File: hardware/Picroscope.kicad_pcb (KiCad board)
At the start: 4 copper layers, 38 x 63.5 mm, 75 parts, among them J1 USB_C_Receptacle_USB2.0_16P, J2 Conn_01x03_Pin, J3 HDMI_A, J4 Conn_02x09_Odd_Even, SW1 SMD_Pushbutton, SW2 SMD_Pushbutton, U1 RP2350B-QFN80, U2 W25Q32JVSS, U3 AMS1117-3.3, Y1 ABM8-272-T3

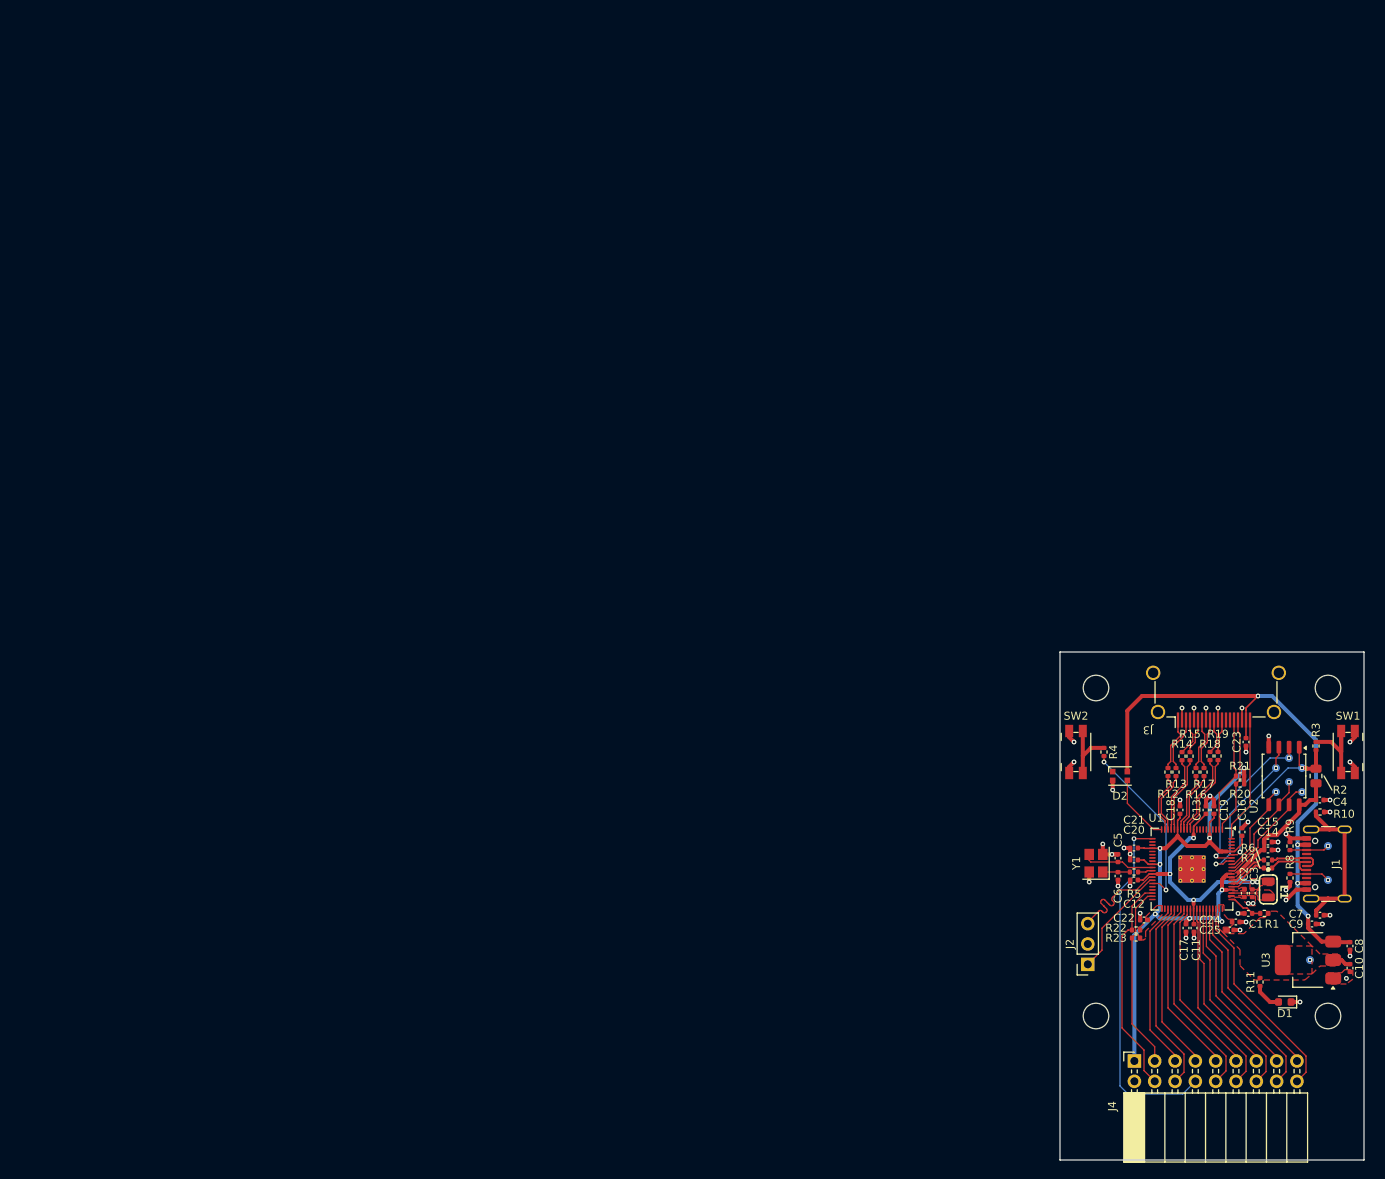
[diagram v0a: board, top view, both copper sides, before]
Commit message: added length tuning to 'crucial' traces except qspi
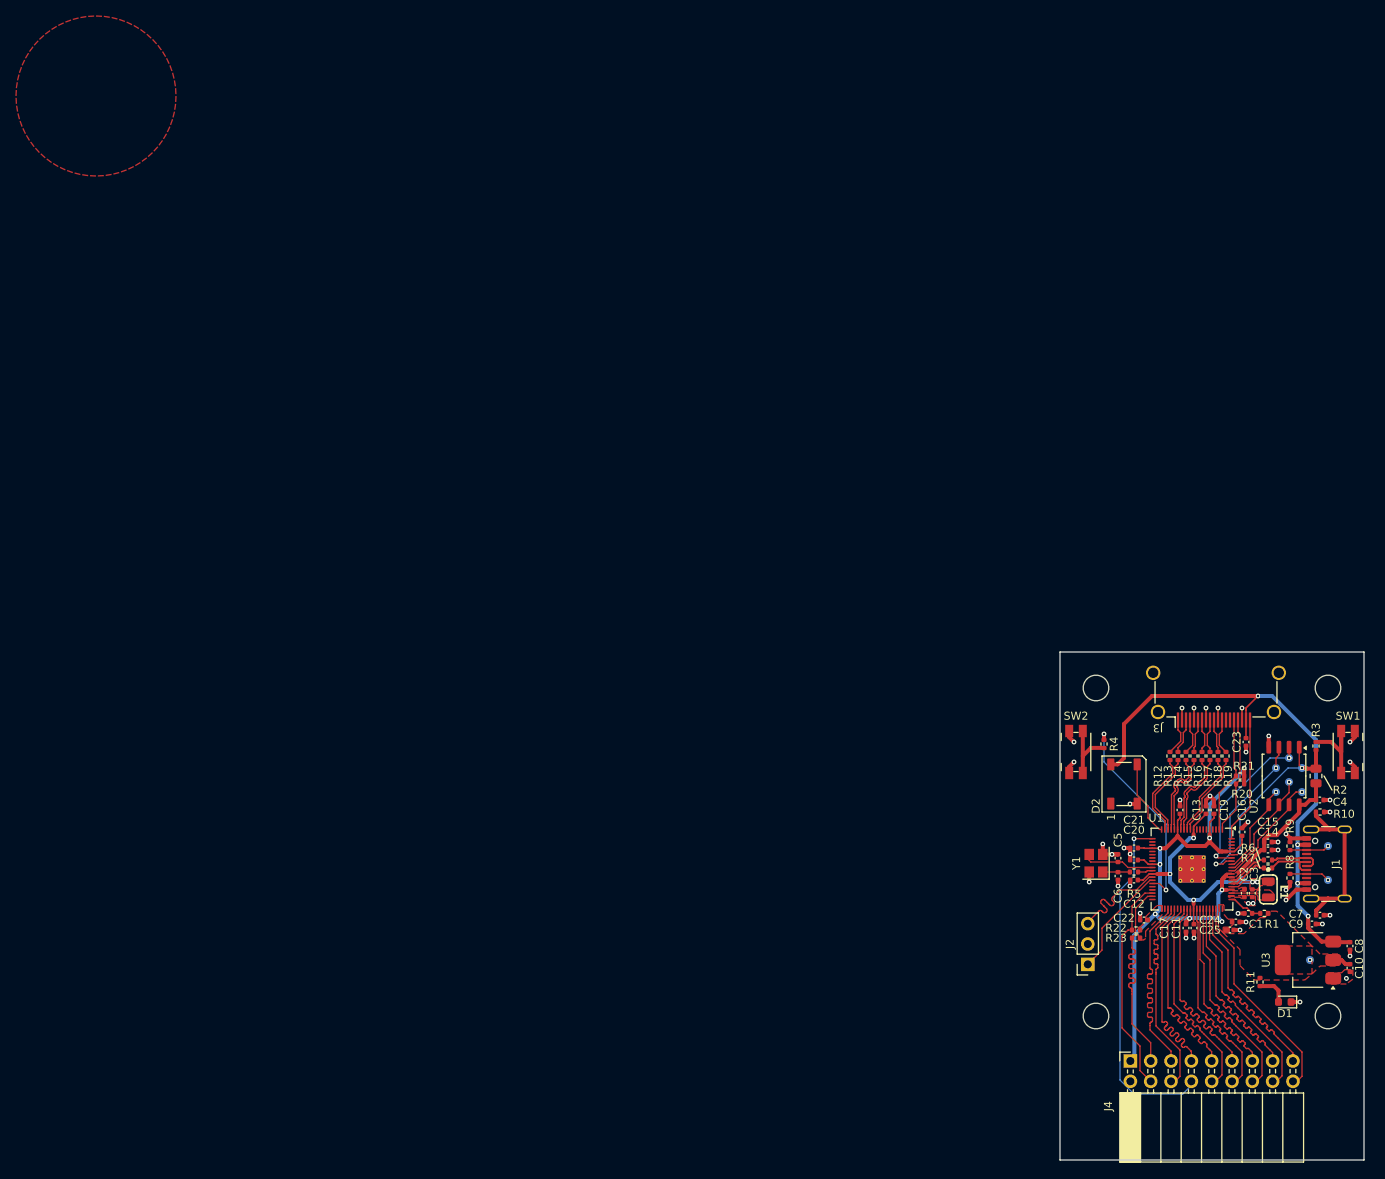
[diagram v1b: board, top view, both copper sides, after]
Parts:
- C7: value 100n -> 100nF
- D2: footprint LED_SMD:LED_WS2812B-2020_PLCC4_2.0x2.0mm -> LED_SMD:LED_WS2812B_PLCC4_5.0x5.0mm_P3.2mm
- moved R16 2.15 mm to (138.2, 82.5)
- moved R17 2.15 mm to (139.2, 82.5)
- moved R12 2.03 mm to (134.2, 82.5)
- moved R13 2.03 mm to (135.2, 82.5)
- moved D2 1.12 mm to (128.5, 86.0), turned to 90 degrees
- moved R18 1.00 mm to (140.2, 82.5)
- moved R19 1.00 mm to (141.2, 82.5)
- moved R4 1.00 mm to (126.0, 81.0), turned to 90 degrees
- moved R14 0.50 mm to (136.2, 82.5)
- moved R15 0.50 mm to (137.2, 82.5)
- moved J4 0.50 mm to (129.3, 120.6)
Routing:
- net /CAM_PCLK: track 21.4 -> 26.6 mm
- net /CAM_VSYNC: track 21.3 -> 26.1 mm
- net /I2C1_SCL: track 23.7 -> 27.7 mm
- net /CAM_D9: track 22.2 -> 26.1 mm
- net /CAM_D7: track 22.3 -> 26.1 mm
- net /MCU/RUN: track 22.0 -> 25.5 mm
- net /CAM_D3: track 22.7 -> 26.2 mm
- net /CAM_D5: track 22.0 -> 25.1 mm
- net /PDVI_D0-: track 7.73 -> 10.6 mm
- net /PDVI_D0+: track 7.73 -> 10.6 mm
- net /CAM_Reset: track 23.4 -> 26.2 mm
- net /PDVI_D2+: track 7.77 -> 10.5 mm
- net /PDVI_D2-: track 7.79 -> 10.5 mm
- net /HDMI_D0+: track 6.59 -> 4.27 mm
- net /HDMI_D0-: track 6.59 -> 4.27 mm
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- added copper zone on F.Cu, net (none)

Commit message: final push for PCB V0.1
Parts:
- added G***: LOGO, LOGO, F.Cu at (137.0, 110.5)
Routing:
- net GND: vias 42 -> 184
- removed copper zone on F.Cu, net (none)
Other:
- board text added: "04/25"
- board text added: "PIcroscope"
- board text added: "ZETT"
- board text added: "hello :)"
- board text added: "tell them"

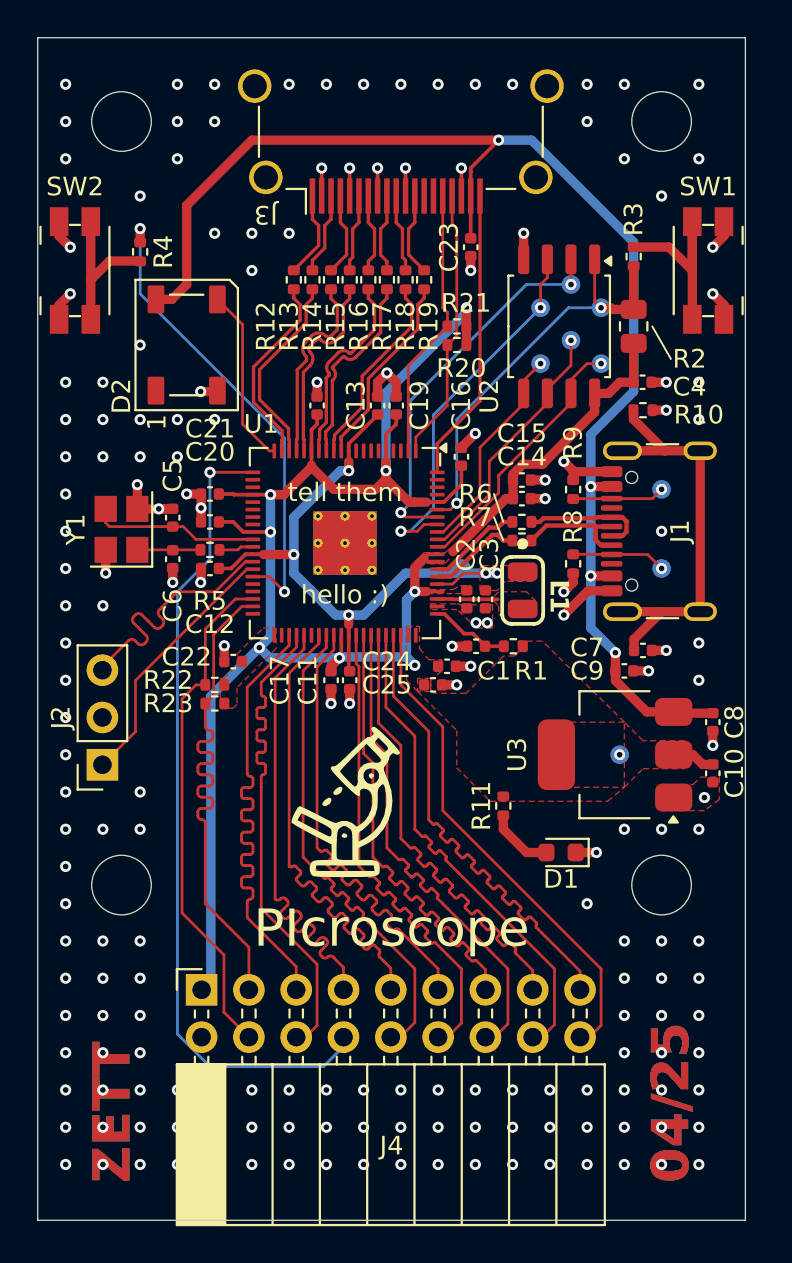
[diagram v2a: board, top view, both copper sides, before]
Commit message: changed C8 & C10 to tantalum caps
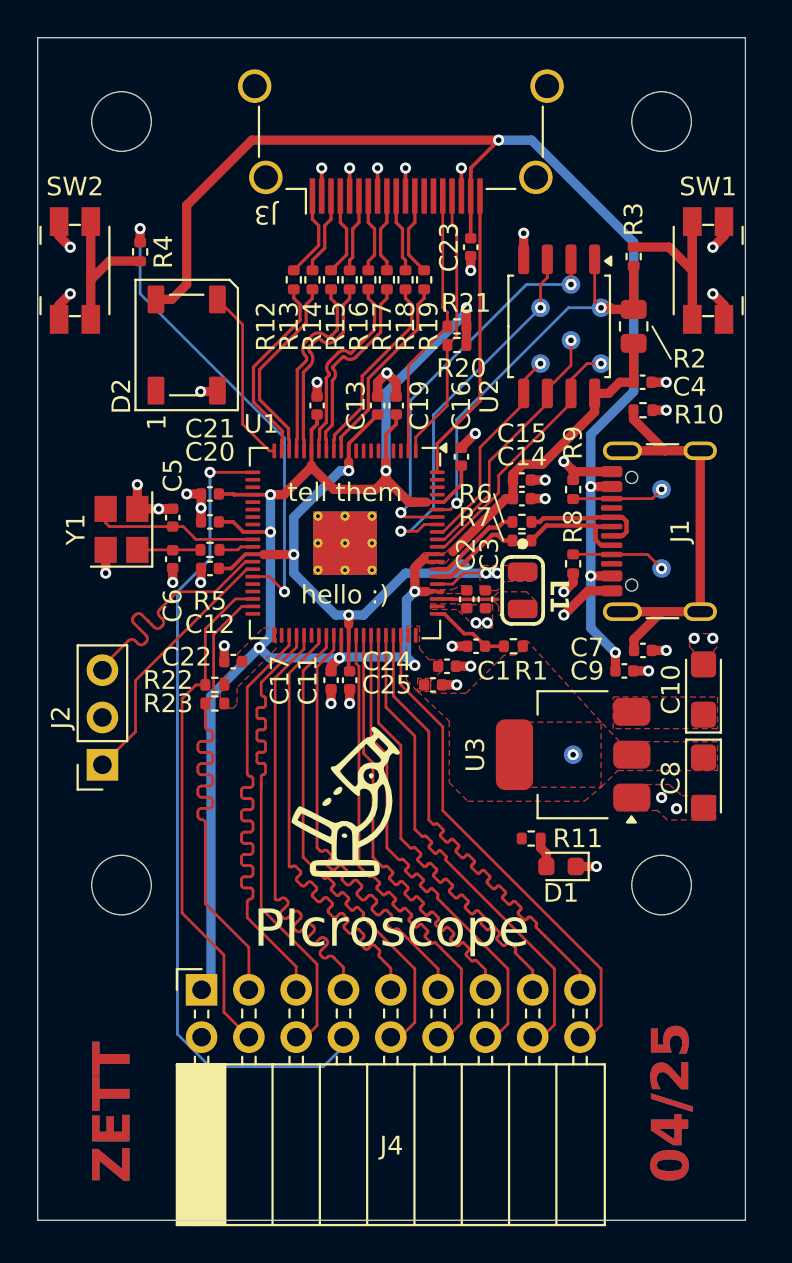
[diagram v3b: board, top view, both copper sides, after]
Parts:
- C10, C8: value 4.7uF -> 22uF; footprint Capacitor_SMD:C_0402_1005Metric -> Capacitor_Tantalum_SMD:CP_EIA-3216-18_Kemet-A
- moved C10 4.53 mm to (156.2, 104.5), turned to 90 degrees
- moved C8 3.29 mm to (156.2, 109.5)
- moved TP8 2.50 mm to (149.2, 108.0)
- moved R11 2.30 mm to (147.0, 112.5), turned to 180 degrees
- moved U3 2.25 mm to (149.2, 108.0)
- moved D1 0.75 mm to (148.6, 114.0)
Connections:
- C10 pad 1: +3V3 -> VBUS
- C8 pad 1: VBUS -> +3V3
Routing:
- net VBUS: track 73.1 -> 66.6 mm
- net +3V3: track 105.2 -> 103.1 mm
- net /PWR_A: track 3.57 -> 1.64 mm
- net GND: track 49.6 -> 48.8 mm, vias 184 -> 44
- added copper zone on F.Cu, net VBUS

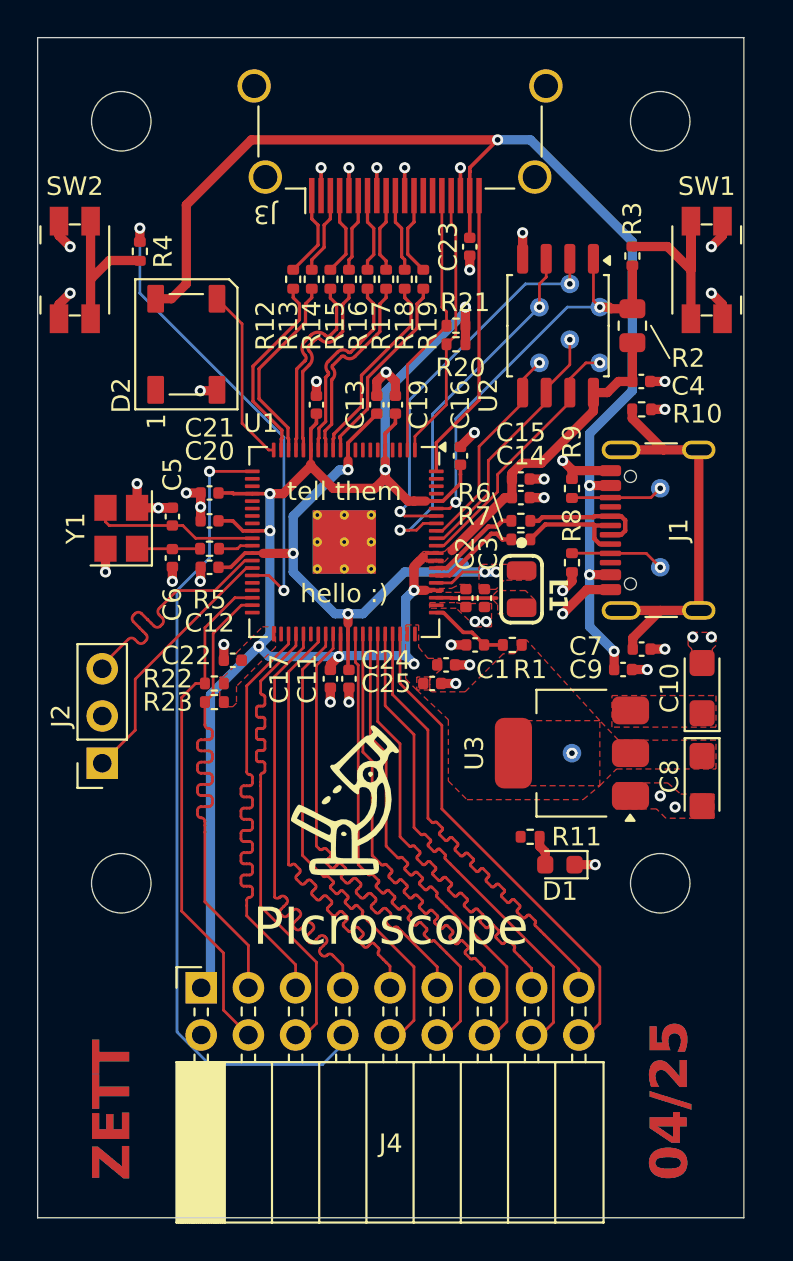
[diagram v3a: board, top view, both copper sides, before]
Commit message: fixed short to GND on CLKOUT0
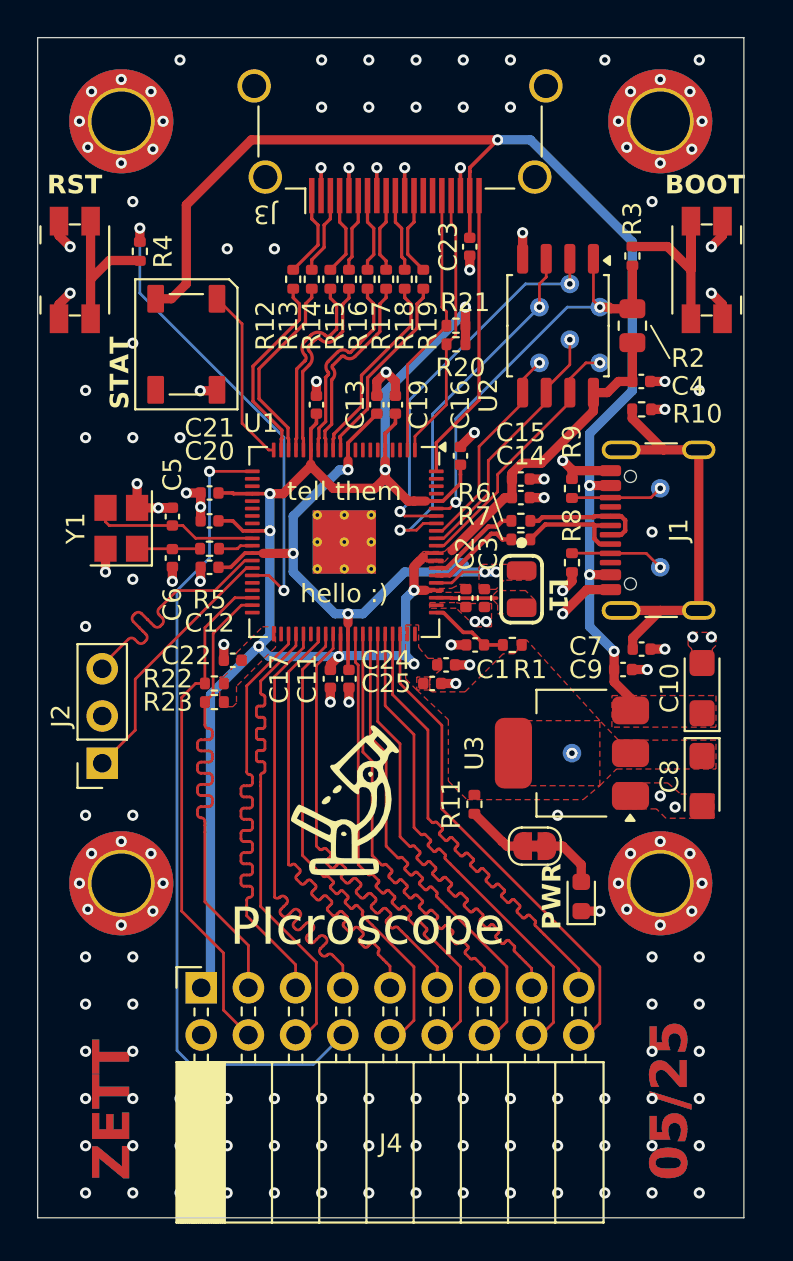
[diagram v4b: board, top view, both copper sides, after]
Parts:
- added JP1: Jumper_2_Bridged, Jumper:SolderJumper-2_P1.3mm_Bridged_RoundedPad1.0x1.5mm, F.Cu at (147.2, 113.0)
- H1, H2, H3, H4: value MountingHole -> MountingHole_Pad; footprint MountingHole:MountingHole_3.2mm_M3_DIN965 -> MountingHole:MountingHole_3.2mm_M3_DIN965_Pad_TopBottom
- moved R11 3.47 mm to (144.0, 110.8), turned to 90 degrees
- moved D1 2.06 mm to (149.8, 115.7), turned to 90 degrees
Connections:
- R11 pad 1: /PWR_A -> Net-(JP1-B)
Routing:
- net Net-(JP1-B): track 0.00 -> 3.32 mm
- net VBUS: track 66.6 -> 69.2 mm
- net /PWR_A: track 1.64 -> 3.19 mm
- net /CLKOUT0: track 44.0 -> 44.6 mm
- net GND: track 48.8 -> 48.7 mm, vias 44 -> 159
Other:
- board text added: "05/25"
- board text added: "BOOT"
- board text added: "PWR"
- board text added: "RST"
- board text added: "STAT"
- board text removed: "04/25"
